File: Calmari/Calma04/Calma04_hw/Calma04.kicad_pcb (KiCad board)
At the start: 2 copper layers, 52.1 x 25 mm, 48 parts, among them Q1 ALS-PT19-315C, SW1 SWITCH, SW2 BUTTON

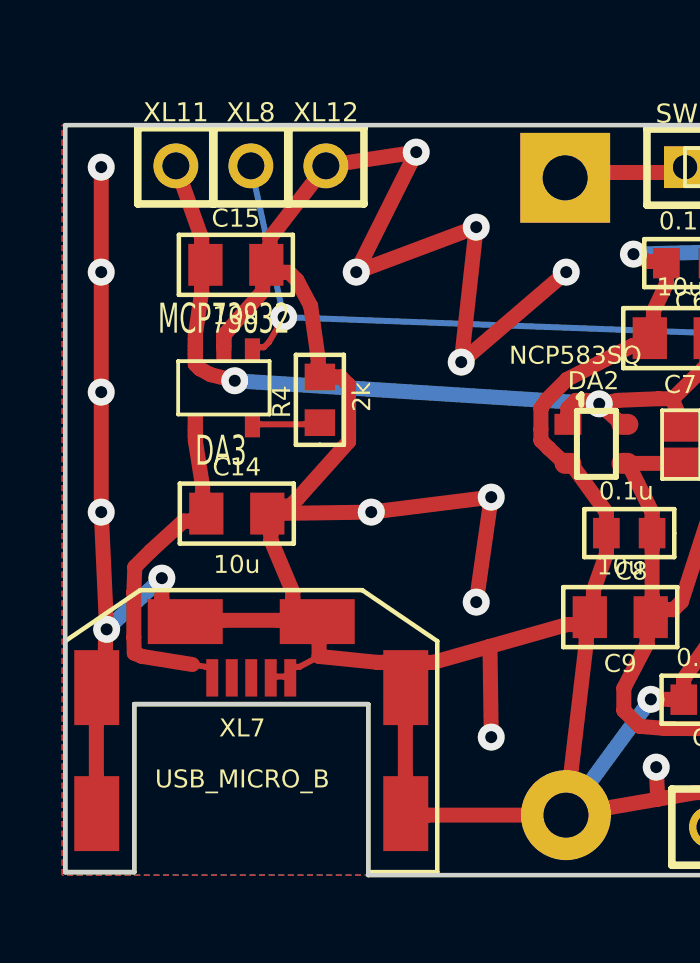
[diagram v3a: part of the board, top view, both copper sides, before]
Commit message: 
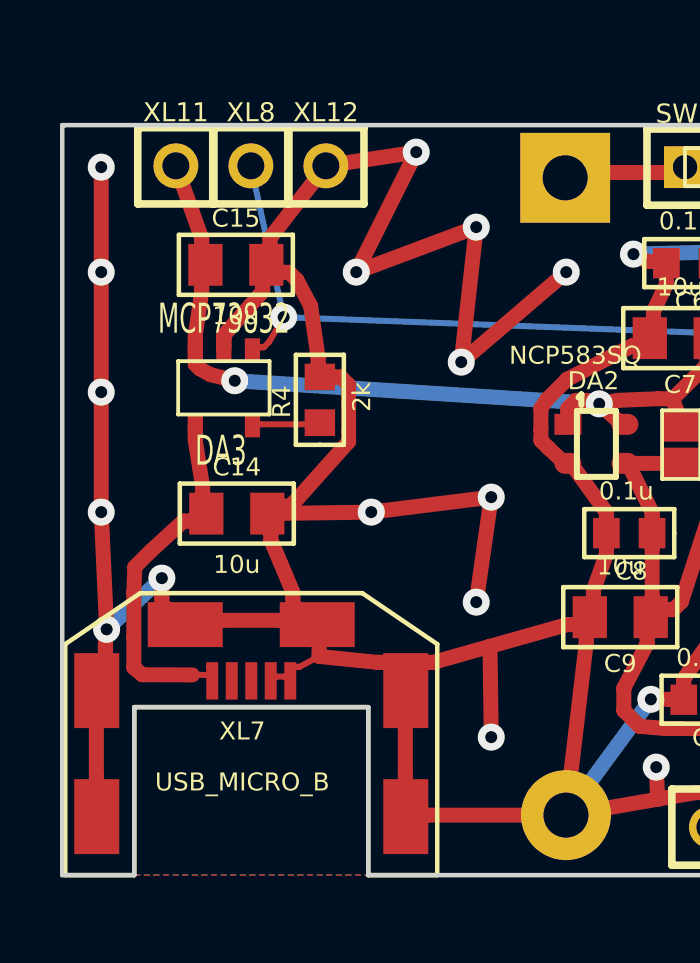
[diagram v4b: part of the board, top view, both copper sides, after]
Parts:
- moved XL7 0.10 mm to (121.5, 144.0)
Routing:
- net +5V: track 11.8 -> 12.7 mm
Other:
- board size 52.1 x 25 mm -> 52.2 x 25 mm
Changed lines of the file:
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@@
     (links 114)
     (no_connects 1)
-    (area 114.638262 121.936727 168.402516 150.50063)
+    (area 114.692262 121.990727 168.348516 150.44663)
     (thickness 1.6)
-    (drawings 9)
+    (drawings 10)
     (tracks 772)
     (zones 0)
@@
   )
   (module USBmicro_MOLEX_WM17142 (layer F.Cu)
-    (at 121.5 143.9 90)
+    (at 121.5 144 90)
     (descr "Molex uUSB, PCB cut needed")
     (fp_text reference XL7 (at -0.8 -0.3 180) (layer F.SilkS)
@@
     )
   )
+  (gr_line (start 115.2 124.6) (end 115.3 124.6) (angle 90) (layer Edge.Cuts) (width 0.15))
+  (gr_line (start 115.2 149.6) (end 115.2 124.6) (angle 90) (layer Edge.Cuts) (width 0.15))
+  (gr_line (start 117.6 149.6) (end 115.2 149.6) (angle 90) (layer Edge.Cuts) (width 0.15))
+  (gr_line (start 117.6 144) (end 117.6 149.6) (angle 90) (layer Edge.Cuts) (width 0.15))
+  (gr_line (start 125.4 144) (end 117.6 144) (angle 90) (layer Edge.Cuts) (width 0.15))
+  (gr_line (start 125.4 149.6) (end 125.4 144) (angle 90) (layer Edge.Cuts) (width 0.15))
   (gr_line (start 115.3 124.6) (end 167.4 124.6) (angle 90) (layer Edge.Cuts) (width 0.15))
-  (gr_line (start 115.3 149.5) (end 115.3 124.6) (angle 90) (layer Edge.Cuts) (width 0.15))
-  (gr_line (start 117.6 149.5) (end 115.3 149.5) (angle 90) (layer Edge.Cuts) (width 0.15))
-  (gr_line (start 117.6 143.9) (end 117.6 149.5) (angle 90) (layer Edge.Cuts) (width 0.15))
-  (gr_line (start 125.4 143.9) (end 117.6 143.9) (angle 90) (layer Edge.Cuts) (width 0.15))
-  (gr_line (start 125.4 149.6) (end 125.4 143.9) (angle 90) (layer Edge.Cuts) (width 0.15))
   (gr_line (start 167.4 149.6) (end 125.4 149.6) (angle 90) (layer Edge.Cuts) (width 0.15))
   (gr_line (start 167.4 124.6) (end 167.4 149.6) (angle 90) (layer Edge.Cuts) (width 0.15))
@@
   (segment (start 143.8968 146.8497) (end 144.1607 147.1136) (width 0.5) (layer F.Cu) (net 1))
   (segment (start 137.35 144.72) (end 143.8968 146.8497) (width 0.5) (layer F.Cu) (net 1))
-  (segment (start 119.9871 142.6567) (end 119.54 142.58) (width 0.2) (layer F.Cu) (net 2))
-  (segment (start 120.0026 137.5484) (end 119.6811 137.7969) (width 0.5) (layer F.Cu) (net 2))
-  (segment (start 119.6811 137.7969) (end 119.4311 137.7969) (width 0.5) (layer F.Cu) (net 2))
-  (segment (start 119.4311 137.7969) (end 119.2447 137.7969) (width 0.5) (layer F.Cu) (net 2))
-  (segment (start 119.2447 137.7969) (end 118.147 138.7995) (width 0.5) (layer F.Cu) (net 2))
-  (segment (start 118.147 138.7995) (end 117.6195 139.327) (width 0.5) (layer F.Cu) (net 2))
-  (segment (start 117.6195 139.327) (end 117.5866 140.1701) (width 0.5) (layer F.Cu) (net 2))
-  (segment (start 117.5866 140.1701) (end 117.5866 141.6701) (width 0.5) (layer F.Cu) (net 2))
-  (segment (start 117.5866 141.6701) (end 117.6 142.2) (width 0.5) (layer F.Cu) (net 2))
-  (segment (start 117.6 142.2) (end 117.8505 142.3072) (width 0.5) (layer F.Cu) (net 2))
-  (segment (start 117.8505 142.3072) (end 119.54 142.58) (width 0.5) (layer F.Cu) (net 2))
+  (segment (start 120.1642 142.9266) (end 119.54 142.9266) (width 0.2) (layer F.Cu) (net 2))
+  (segment (start 120.0871 142.6567) (end 120.1642 142.9266) (width 0.2) (layer F.Cu) (net 2))
   (segment (start 120.1871 142.9817) (end 120.0871 142.6567) (width 0.2) (layer F.Cu) (net 2))
-  (segment (start 120.0871 142.6567) (end 119.9871 142.6567) (width 0.2) (layer F.Cu) (net 2))
   (segment (start 119.8816 137.0999) (end 120.0026 137.5484) (width 0.5) (layer F.Cu) (net 2))
   (segment (start 119.8816 136.8499) (end 119.8816 137.0999) (width 0.5) (layer F.Cu) (net 2))
@@
   (segment (start 119.6346 134.7577) (end 119.6346 135.0077) (width 0.5) (layer F.Cu) (net 2))
   (segment (start 119.6346 134.6267) (end 119.6346 134.7577) (width 0.5) (layer F.Cu) (net 2))
+  (segment (start 117.8734 142.9211) (end 119.54 142.9266) (width 0.5) (layer F.Cu) (net 2))
+  (segment (start 117.5864 142.6829) (end 117.8734 142.9211) (width 0.5) (layer F.Cu) (net 2))
+  (segment (start 117.5866 141.6701) (end 117.5864 142.6829) (width 0.5) (layer F.Cu) (net 2))
+  (segment (start 117.5866 140.1701) (end 117.5866 141.6701) (width 0.5) (layer F.Cu) (net 2))
+  (segment (start 117.6195 139.327) (end 117.5866 140.1701) (width 0.5) (layer F.Cu) (net 2))
+  (segment (start 118.147 138.7995) (end 117.6195 139.327) (width 0.5) (layer F.Cu) (net 2))
+  (segment (start 119.2447 137.7969) (end 118.147 138.7995) (width 0.5) (layer F.Cu) (net 2))
+  (segment (start 119.4311 137.7969) (end 119.2447 137.7969) (width 0.5) (layer F.Cu) (net 2))
+  (segment (start 119.6811 137.7969) (end 119.4311 137.7969) (width 0.5) (layer F.Cu) (net 2))
+  (segment (start 120.0026 137.5484) (end 119.6811 137.7969) (width 0.5) (layer F.Cu) (net 2))
   (via (at 120.95 133.12) (size 0.9) (layers F.Cu B.Cu) (net 3))
   (via (at 133.1 133.89) (size 0.9) (layers F.Cu B.Cu) (net 3))
